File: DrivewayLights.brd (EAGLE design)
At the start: 69.8 x 69.8 mm, 61 parts, among them U0 F22X4---DA38, U1 TLC59108PW, U3 A1101, U4 TPS62111RSA

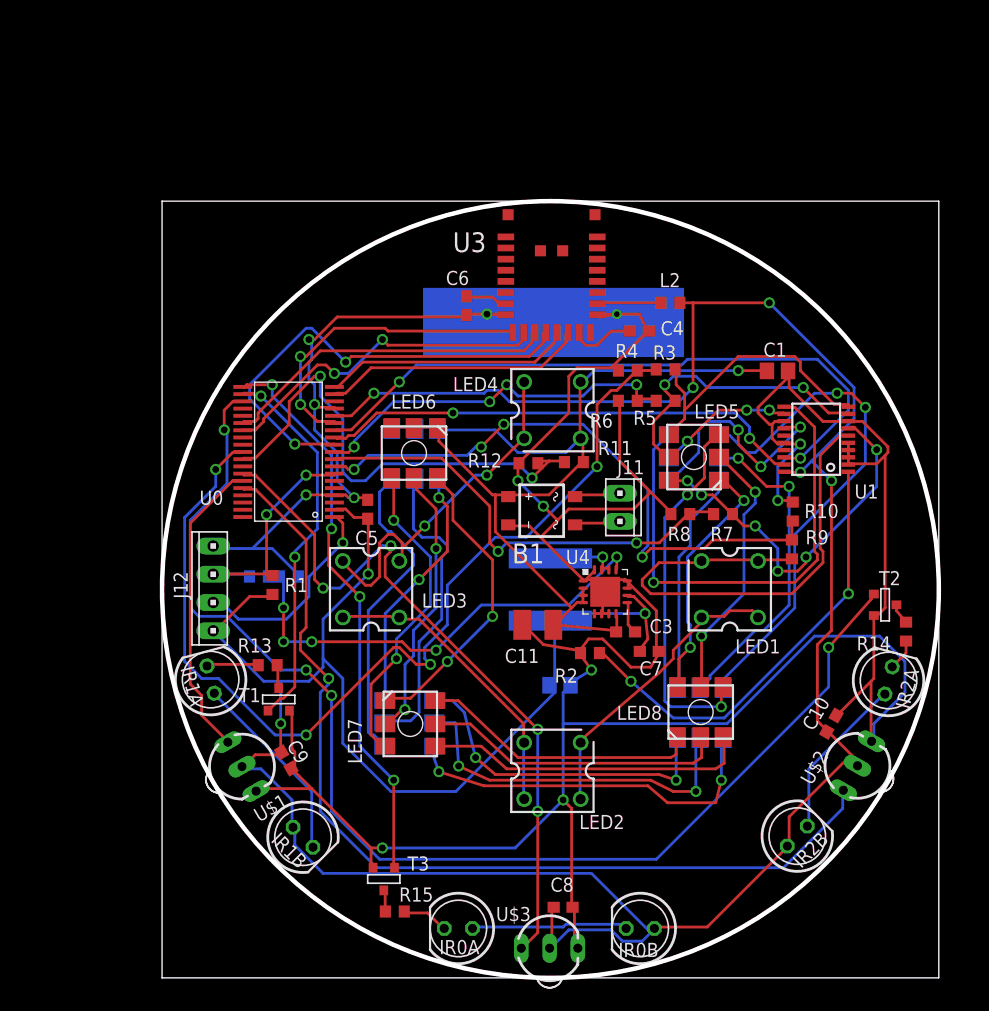
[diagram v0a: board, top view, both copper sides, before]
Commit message: First pass at adding the Photon board
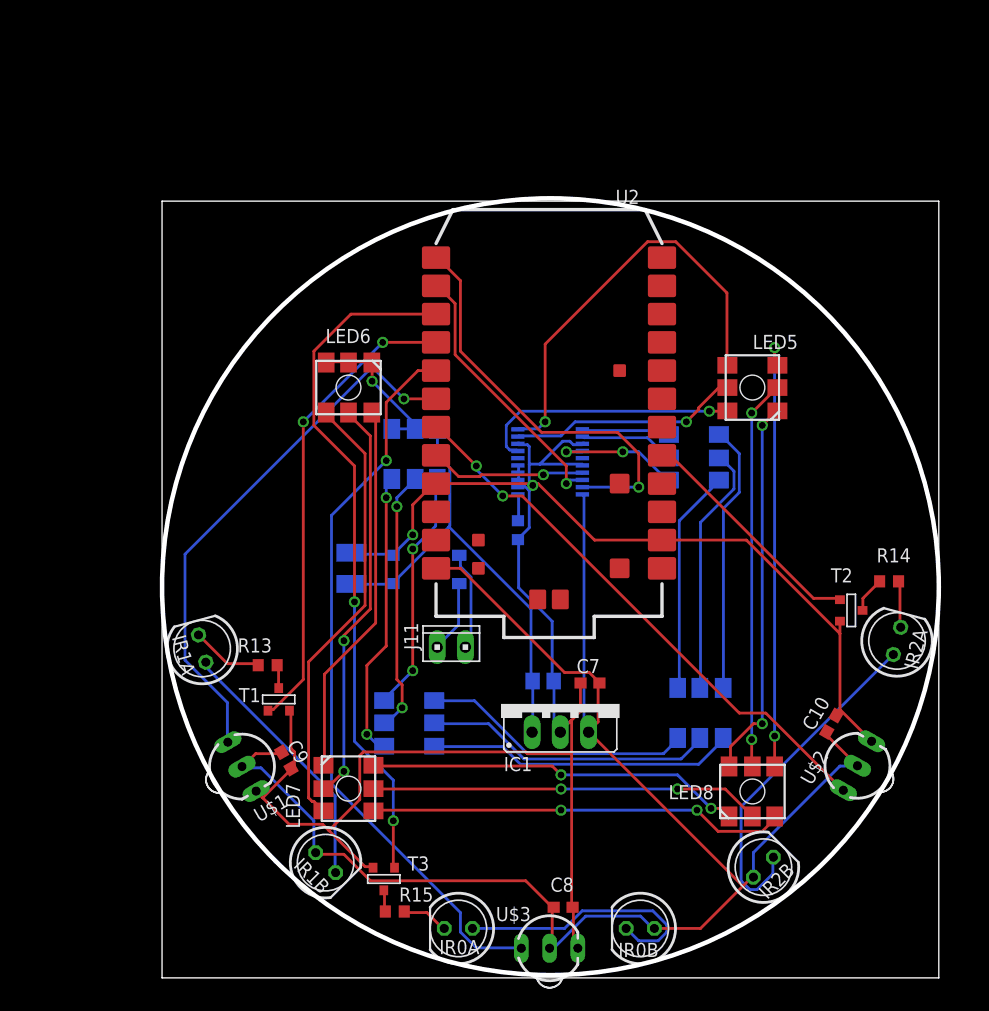
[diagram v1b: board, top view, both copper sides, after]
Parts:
- removed C2: 22uF, rcl:C0805
- removed C3: 1uF, rcl:C0603
- removed C4, C5, C6: (no value), rcl:C0603
- removed J1, J2, L2: (no value), rcl:R0603
- removed J12: (no value), con-amp:10X04MTA
- removed L1: NRS8030, inductors:NRS8030
- removed LED1, LED2, LED3, LED4: (no value), led:SUPERFLUX-7.6X7.6
- removed R1: 47k, rcl:R0603
- removed R10, R12, R4, R6, R8: 10k, rcl:R0603
- removed R11, R3, R5, R7, R9: 51k, rcl:R0603
- removed U0: F22X4---DA38, TI_MSP430_v16:DA38
- removed U3: A1101, anaren:A1101
- removed U4: TPS62111RSA, texas2:S-PVQFN-N16
- added IC1: (no value), v-reg:78XXS
- added U2: PHOTON_SMD, Spark:PHOTON_SMD
- moved C1 35.0 mm to (34.3, 26.7), flipped to the bottom, turned to 180 degrees
- moved U1 24.0 mm to (34.9, 46.4), flipped to the bottom
- moved J11 19.7 mm to (26.0, 29.7), turned to 0 degrees
- moved C11 17.5 mm to (17.0, 36.8), flipped to the bottom, turned to 90 degrees
- moved R2 12.8 mm to (32.0, 40.3), flipped to the bottom, turned to 90 degrees
- moved B1 11.7 mm to (23.7, 36.7), flipped to the bottom, turned to 90 degrees
- moved LED8 8.52 mm to (53.1, 16.8)
- moved LED6 8.33 mm to (16.8, 53.1)
- moved LED5 8.17 mm to (53.1, 53.1)
- moved LED7 8.05 mm to (16.8, 17.0)
- moved C7 6.05 mm to (38.5, 26.5), turned to 180 degrees
- moved R14 4.77 mm to (65.4, 35.7), turned to 0 degrees
- moved IR2B 4.13 mm to (54.1, 9.96)
- moved IR2A 3.64 mm to (66.1, 30.3)
- moved T2 3.09 mm to (62.0, 33.0)
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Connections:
- net N$19 renamed LED_CURRENT_R
- removed net !RF_CE: U0.11, U3.12
- removed net N$10: LED1.1, LED1.3, R9.2, U1.6
- removed net N$34: LED1.2, LED1.4, LED2.1, LED2.3
- removed net N$35: LED2.2, LED2.4, LED3.1, LED3.3
- removed net N$36: LED3.2, LED3.4, LED4.1, LED4.3
- removed net N$38: U1.17
- removed net N$42: L2.2, U3.18
- removed net N$7: U0.38
- removed net N$8: C3.2, U4.9
- removed net PG: J1.1, J2.2, U4.13
- removed net RESET/SBWTDIO: J1.2, J12.2, R1.1, U0.7
- removed net RF_CLK: U0.14, U3.9
- removed net RF_GDO0: U0.19, U3.13
- removed net RF_GDO2: U0.18, U3.14
- removed net RF_SIMO: U0.25, U3.11
- removed net RF_SOMI: U0.26, U3.10
- removed net SBWTCK: J12.3, U0.1
- removed net VBLUE_SCALED: R3.1, R4.2, U0.29
- removed net VDCOUP1: C6.1, U3.7
- removed net VDCOUP2: C4.1, U3.15
- removed net VGREEN_SCALED: R5.1, R6.2, U0.10
- removed net VIN: B1.+, C1.1, C11.1, C3.1, LED10.1, LED10.2, LED10.3, LED4.2, LED4.4, LED6.1, LED6.2, LED6.3, R11.2, U4.2, U4.3, U4.4, U4.8
- removed net VIN_SCALED: R11.1, R12.2, U0.30
- removed net VRED_SCALED: R7.1, R8.2, U0.9
- removed net VWHITE_SCALED: R10.2, R9.1, U0.8
- new net LED_NRESET: U1.17, U2.20
- new net VBAT: U2.22
- new net VCAP: B1.+, C1.1, C11.1, IC1.IN, LED10.1, LED10.2, LED10.3, LED6.1, LED6.2, LED6.3
- net 3.3V: now also IC1.OUT, U2.24; no longer C2.1, C5.1, J12.4, L1.2, L2.1, R1.2, U0.15, U0.2, U4.10
- net BLUE: no longer R3.2
- net GND: now also IC1.GND, U2.2, U2.21; no longer C2.2, C4.2, C5.2, C6.2, J12.1, J2.1, R10.1, R12.1, R4.1, R6.1, R8.1, U0.16, U0.4, U3.17, U3.8, U4.1, U4.11, U4.12, U4.16, U4.5, U4.6, U4.7, U4.TH
- net GREEN: no longer R5.2
- net IRLED0: now also U2.15; no longer U0.20
- net IRLED1: now also U2.16; no longer U0.21
- net IRLED2: now also U2.5; no longer U0.22
- net IR_IN0: now also U2.17; no longer U0.32
- net IR_IN1: now also U2.18; no longer U0.33
- net IR_IN2: now also U2.19; no longer U0.34
- net LED_SCL: now also U2.14; no longer U0.13
- net LED_SDA: now also U2.13; no longer U0.12
- net N$1: now also U2.1; no longer L1.1, U4.14, U4.15
- net RED: no longer R7.2
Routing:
- net GND: track 357.0 -> 185.1 mm, vias 13 -> 2
- net 3.3V: track 293.2 -> 148.9 mm, vias 8 -> 0
- net VIN: track 90.3 -> 0.00 mm, vias 1 -> 0
- net IRLED2: track 110.4 -> 21.4 mm, vias 4 -> 0
- net VBLUE_SCALED: track 88.5 -> 0.00 mm, vias 4 -> 0
- net VCAP: track 0.00 -> 58.3 mm, vias 0 -> 1
- net VWHITE_SCALED: track 54.5 -> 0.00 mm, vias 4 -> 0
- net N$10: track 45.8 -> 0.00 mm
- net VIN_SCALED: track 43.9 -> 0.00 mm, vias 2 -> 0
- net PG: track 42.3 -> 0.00 mm, vias 5 -> 0
- net !RF_CE: track 42.2 -> 0.00 mm, vias 2 -> 0
- net VRED_SCALED: track 41.2 -> 0.00 mm, vias 2 -> 0
- net LED_CURRENT_R: track 40.6 -> 2.44 mm, vias 2 -> 0
- net RED2: track 45.0 -> 7.97 mm, vias 1 -> 0
- net IR_IN2: track 86.5 -> 50.3 mm, vias 1 -> 2
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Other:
- board size 69.8 x 69.8 mm -> 69.8 x 70.1 mm

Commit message: Some layout cleanup
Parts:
- moved C8 1.27 mm to (36.1, 7.62)
- moved U$3 1.05 mm to (35.1, 3.68)
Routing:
- net GND: track 185.1 -> 89.9 mm, vias 2 -> 1
- net IR_IN1: track 49.0 -> 63.6 mm, vias 1 -> 2
- net N$23: track 23.8 -> 16.3 mm
- net IR_IN0: track 66.2 -> 65.1 mm
- net 3.3V: track 148.9 -> 148.0 mm
- added copper zone on layer 16, net GND

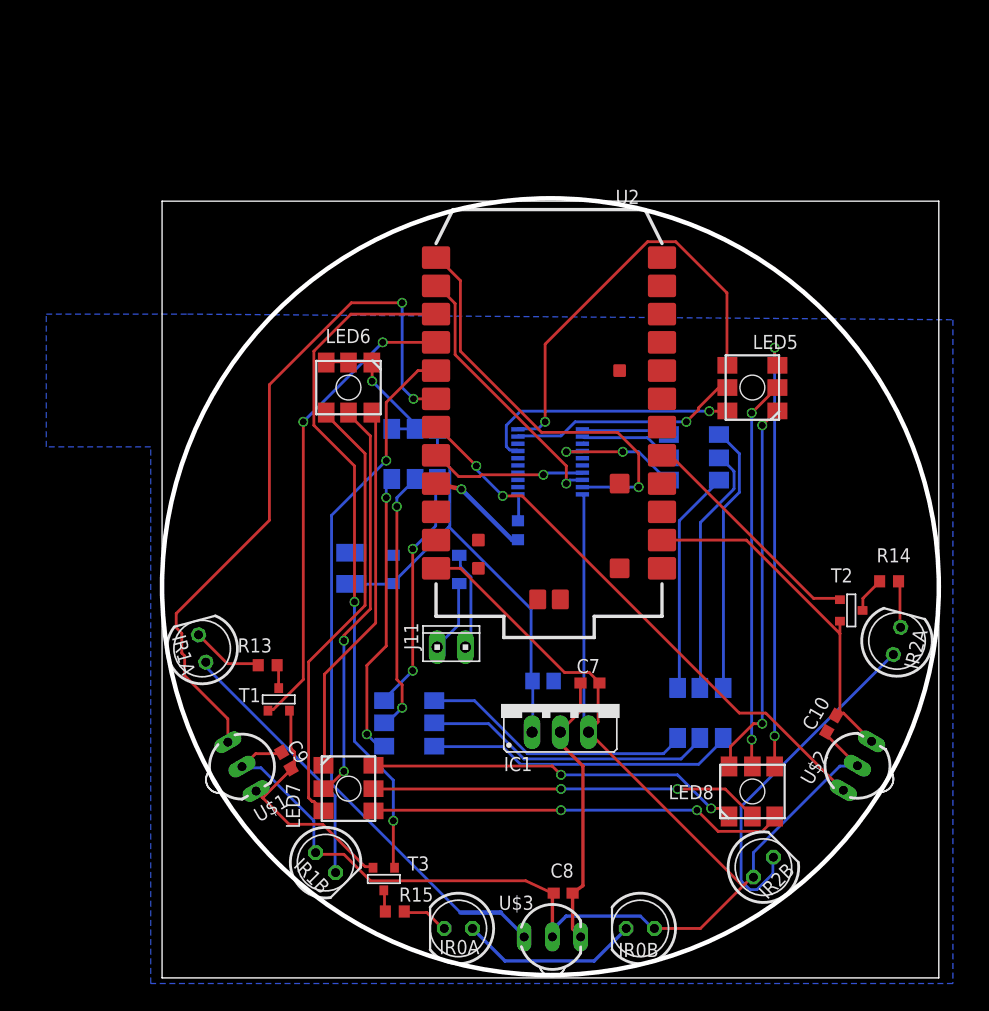
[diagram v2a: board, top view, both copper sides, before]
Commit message: Updated Board design to test new size to just fit into bottom bulge. Adding 3d models
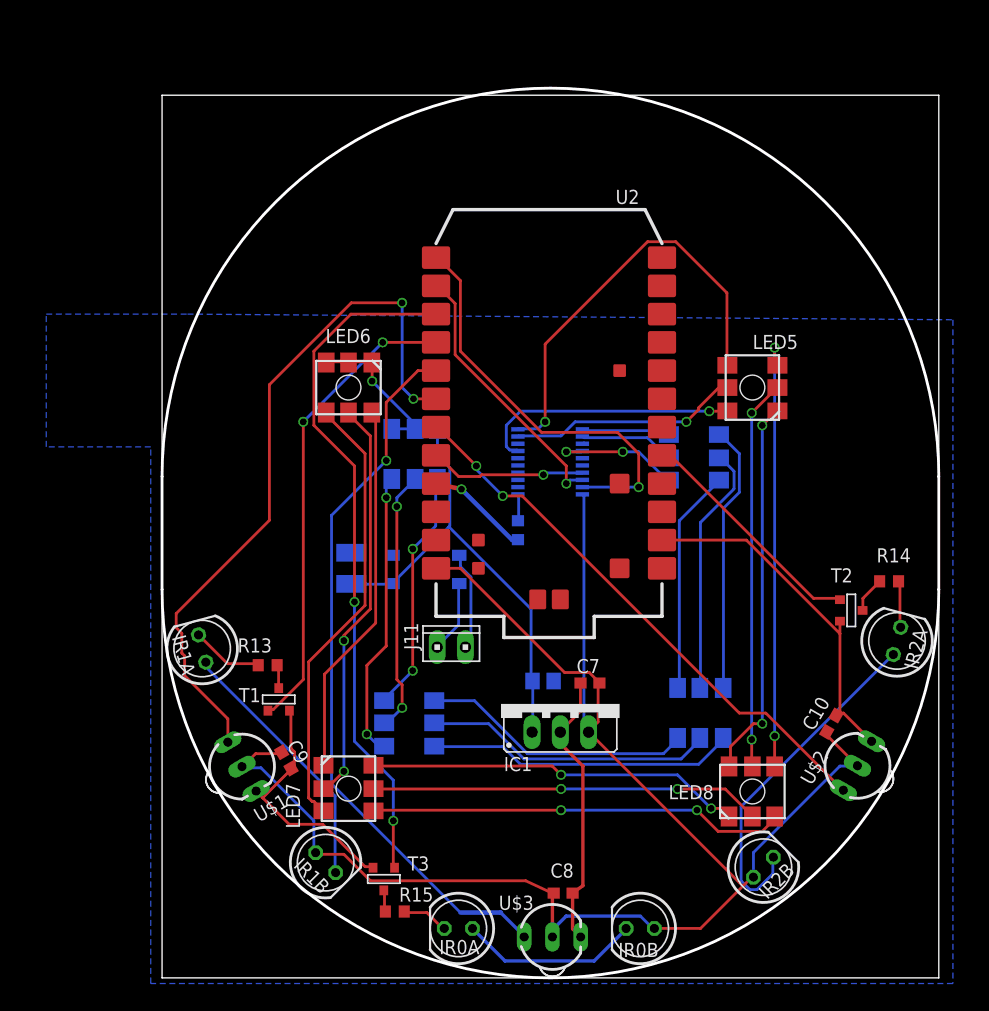
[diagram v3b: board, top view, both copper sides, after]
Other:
- board size 69.8 x 70.1 mm -> 69.8 x 80 mm
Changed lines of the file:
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@@
 <?xml version="1.0" encoding="utf-8"?>
 <!DOCTYPE eagle SYSTEM "eagle.dtd">
-<eagle version="7.2.0">
+<eagle version="7.6.0">
 <drawing>
 <settings>
@@
 <setting verticaltext="up"/>
 </settings>
-<grid distance="0.01" unitdist="inch" unit="inch" style="lines" multiple="1" display="yes" altdistance="0.025" altunitdist="inch" altunit="inch"/>
+<grid distance="0.005" unitdist="inch" unit="inch" style="lines" multiple="1" display="yes" altdistance="0.025" altunitdist="inch" altunit="inch"/>
 <layers>
 <layer number="1" name="Top" color="4" fill="1" visible="yes" active="yes"/>
@@
 <plain>
 <wire x1="0" y1="0" x2="69.85" y2="0" width="0" layer="20"/>
-<wire x1="69.85" y1="0" x2="69.85" y2="69.85" width="0" layer="20"/>
-<wire x1="69.85" y1="69.85" x2="0" y2="69.85" width="0" layer="20"/>
-<wire x1="0" y1="69.85" x2="0" y2="0" width="0" layer="20"/>
-<circle x="34.925" y="35.179" radius="34.925" width="0.4064" layer="20"/>
+<wire x1="69.85" y1="0" x2="69.85" y2="34.925" width="0" layer="20"/>
+<wire x1="69.85" y1="45.085" x2="69.85" y2="79.375" width="0" layer="20"/>
+<wire x1="69.85" y1="79.375" x2="0" y2="79.375" width="0" layer="20"/>
+<wire x1="0" y1="79.375" x2="0" y2="45.085" width="0" layer="20"/>
 <circle x="34.925" y="34.925" radius="25.4" width="0.4064" layer="19"/>
 <rectangle x1="12.9794" y1="62.23" x2="56.3626" y2="70.0532" layer="42"/>
+<wire x1="0" y1="34.925" x2="0" y2="0" width="0" layer="20"/>
+<wire x1="69.85" y1="34.925" x2="0" y2="34.925" width="0.254" layer="20" curve="-180"/>
+<wire x1="0" y1="45.085" x2="69.85" y2="45.085" width="0.254" layer="20" curve="-180"/>
+<wire x1="0" y1="34.925" x2="0" y2="45.085" width="0.254" layer="20"/>
+<wire x1="69.85" y1="45.085" x2="69.85" y2="34.925" width="0.254" layer="20"/>
 </plain>
 <attributes>

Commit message: Changed to using ESP8266 board and started laying out board.
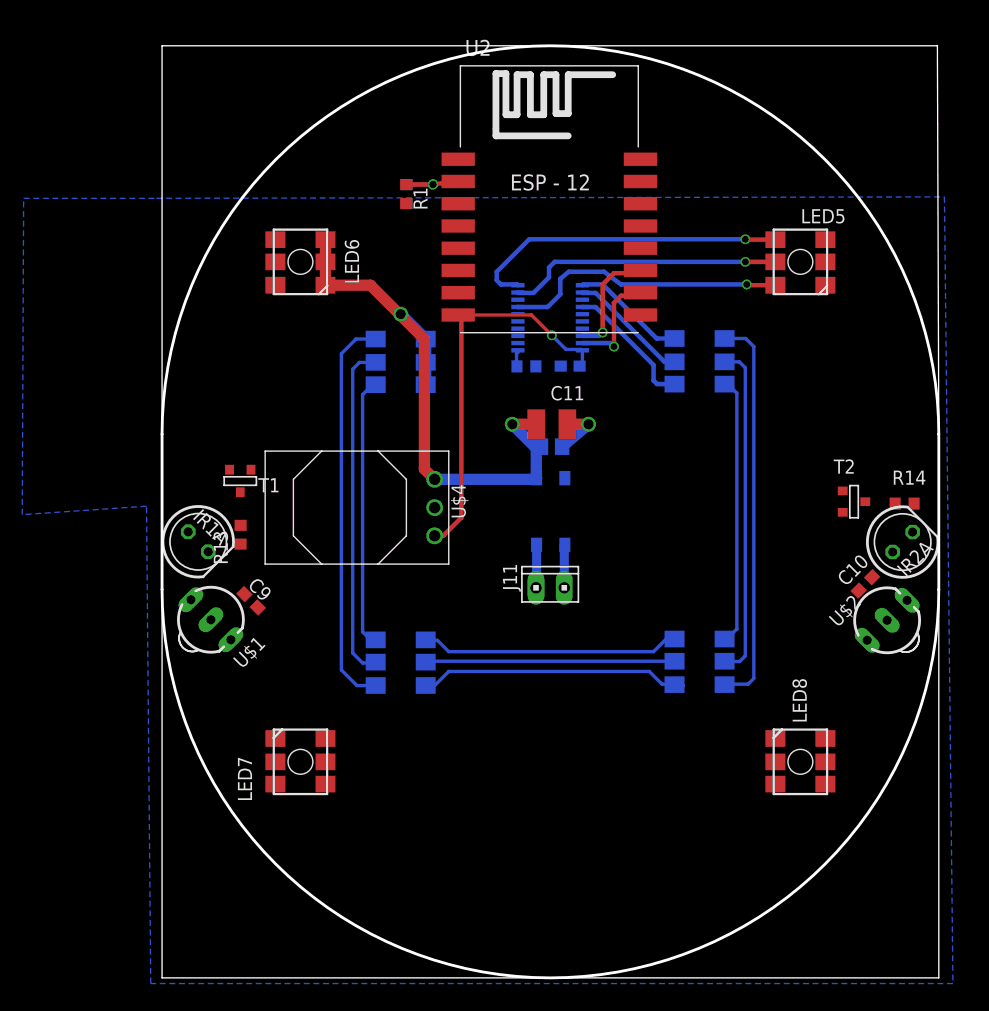
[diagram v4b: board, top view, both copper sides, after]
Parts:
- removed C8: (no value), rcl:C0603
- removed IC1: (no value), v-reg:78XXS
- removed IR0A, IR0B, IR1B, IR2B: (no value), led:LED5MM
- removed R15: 10, rcl:R0603
- removed T3: (no value), zetex:SOT-23
- removed U$3: TSOP39338, opto-vishay:TSOP39338
- added R1: 24k, resistor:R0603
- added R3: 1k, resistor:R0603
- added U$4: DCDC_OKI-78SR, rwt-library:OKI-78SRH
- U2: value PHOTON_SMD -> (none); device Spark:PHOTON_SMD -> esp8266modules:ESP12-SMD
- moved C7 28.6 mm to (36.7, 55.0), flipped to the bottom, turned to 0 degrees
- moved C11 22.2 mm to (35.1, 49.8), flipped to the top, turned to 0 degrees
- moved C1 21.1 mm to (35.0, 47.8)
- moved T1 19.9 mm to (7.01, 44.7), turned to 0 degrees
- moved R2 14.8 mm to (32.8, 55.0), turned to 0 degrees
- moved C9 14.7 mm to (8.00, 33.9), turned to 315 degrees
- moved U$1 13.5 mm to (4.39, 32.2), turned to 315 degrees
- moved U$2 13.4 mm to (65.2, 32.2), turned to 45 degrees
- moved U1 13.0 mm to (34.9, 59.4)
- moved C10 12.9 mm to (63.2, 35.4), turned to 45 degrees
- moved B1 12.4 mm to (35.0, 41.9), turned to 180 degrees
- moved LED5 12.1 mm to (57.4, 64.4)
- moved LED6 12.1 mm to (12.4, 64.4), turned to 180 degrees
- moved R13 12.0 mm to (7.06, 39.9), turned to 270 degrees
- moved J11 10.4 mm to (34.9, 35.1)
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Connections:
- removed net IRLED0: T3.3, U2.15
- removed net IR_IN0: U$3.OUT, U2.17
- removed net N$1: U2.1
- removed net N$22: IR0A.K, R15.2
- removed net N$23: IR0A.A, IR0B.K
- removed net N$24: R15.1, T3.1
- removed net N$3: IR2A.A, IR2B.K
- removed net N$4: IR1A.A, IR1B.K
- removed net VBAT: U2.22
- new net N$7: R1.1, R3.2, U2.ADC
- net 3.3V: now also IR1A.A, IR2A.A, U$4.3, U2.VCC; no longer C8.1, IC1.OUT, IR0B.A, IR1B.A, IR2B.A, U$3.VS, U2.24
- net GND: now also R3.1, U$4.2, U2.GND; no longer C8.2, IC1.GND, T3.2, U$3.GND, U2.2, U2.21
- net IRLED1: no longer U2.16
- net IRLED2: no longer U2.5
- net IR_IN1: no longer U2.18
- net IR_IN2: no longer U2.19
- net LED_NRESET: no longer U2.20
- net LED_SCL: now also U2.GPIO2; no longer U2.14
- net LED_SDA: now also U2.GPIO15; no longer U2.13
- net VCAP: now also R1.2, U$4.1; no longer IC1.IN
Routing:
- net 3.3V: track 148.0 -> 35.5 mm, vias 0 -> 1
- net GND: track 89.9 -> 5.01 mm
- net IR_IN0: track 65.1 -> 0.00 mm, vias 1 -> 0
- net IR_IN1: track 63.6 -> 0.00 mm, vias 2 -> 0
- net IRLED0: track 61.8 -> 0.00 mm, vias 2 -> 0
- net IR_IN2: track 50.3 -> 0.00 mm, vias 2 -> 0
- net IRLED1: track 42.5 -> 0.00 mm, vias 2 -> 0
- net N$27: track 40.1 -> 0.00 mm
- net N$25: track 39.4 -> 0.00 mm, vias 2 -> 0
- net N$26: track 37.6 -> 0.00 mm, vias 2 -> 0
- net N$28: track 36.7 -> 0.00 mm, vias 2 -> 0
- net N$29: track 35.1 -> 0.00 mm, vias 2 -> 0
- net N$30: track 35.1 -> 0.00 mm, vias 2 -> 0
- net N$31: track 34.3 -> 0.00 mm, vias 2 -> 0
- net N$32: track 33.9 -> 0.00 mm, vias 2 -> 0
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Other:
- board size 69.8 x 80 mm -> 69.8 x 83.8 mm

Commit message: Updated to a fully routed board.  Could have some bugs, needs electrical and mechanical review
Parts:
- moved R3 3.29 mm to (19.1, 69.0), flipped to the top, turned to 0 degrees
- moved R1 3.14 mm to (18.9, 71.2), turned to 180 degrees
- moved R14 0.90 mm to (66.6, 43.5)
- moved T2 0.77 mm to (62.4, 43.6)
- moved R13 0.51 mm to (7.57, 39.9)
- moved T1 0.38 mm to (7.39, 44.7)
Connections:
- net IRLED1: now also U2.GPIO12
- net IRLED2: now also U2.GPIO5
- net IR_IN1: now also U2.GPIO13
- net IR_IN2: now also U2.GPIO0
- net LED_NRESET: now also U2.GPIO14
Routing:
- net GND: track 5.01 -> 93.6 mm, vias 1 -> 4
- net 3.3V: track 35.5 -> 118.2 mm, vias 1 -> 2
- net N$25: track 0.00 -> 61.0 mm, vias 0 -> 2
- net N$27: track 0.00 -> 58.1 mm, vias 0 -> 2
- net N$30: track 0.00 -> 56.1 mm, vias 0 -> 2
- net N$28: track 0.00 -> 54.1 mm, vias 0 -> 2
- net IR_IN2: track 0.00 -> 48.7 mm, vias 0 -> 2
- net N$31: track 0.00 -> 46.9 mm, vias 0 -> 2
- net N$33: track 0.00 -> 45.8 mm, vias 0 -> 2
- net N$32: track 0.00 -> 40.5 mm
- net N$29: track 0.00 -> 40.5 mm
- net N$26: track 0.00 -> 40.5 mm
- net IR_IN1: track 0.00 -> 40.2 mm, vias 0 -> 1
- net IRLED2: track 0.00 -> 33.8 mm
- net IRLED1: track 0.00 -> 27.8 mm
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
